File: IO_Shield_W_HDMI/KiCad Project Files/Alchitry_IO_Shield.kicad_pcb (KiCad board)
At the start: 4 copper layers, 65 x 45 mm, 67 parts, among them J1 HDMI_A_1.4, Q1 Q_PMOS_SGD, Q2 Q_PMOS_SGD, Q3 Q_PMOS_SGD, SW1 SW_DIP_x08, SW2 SW_DIP_x08, U1 boardmezzanine_new, U2 TFP410

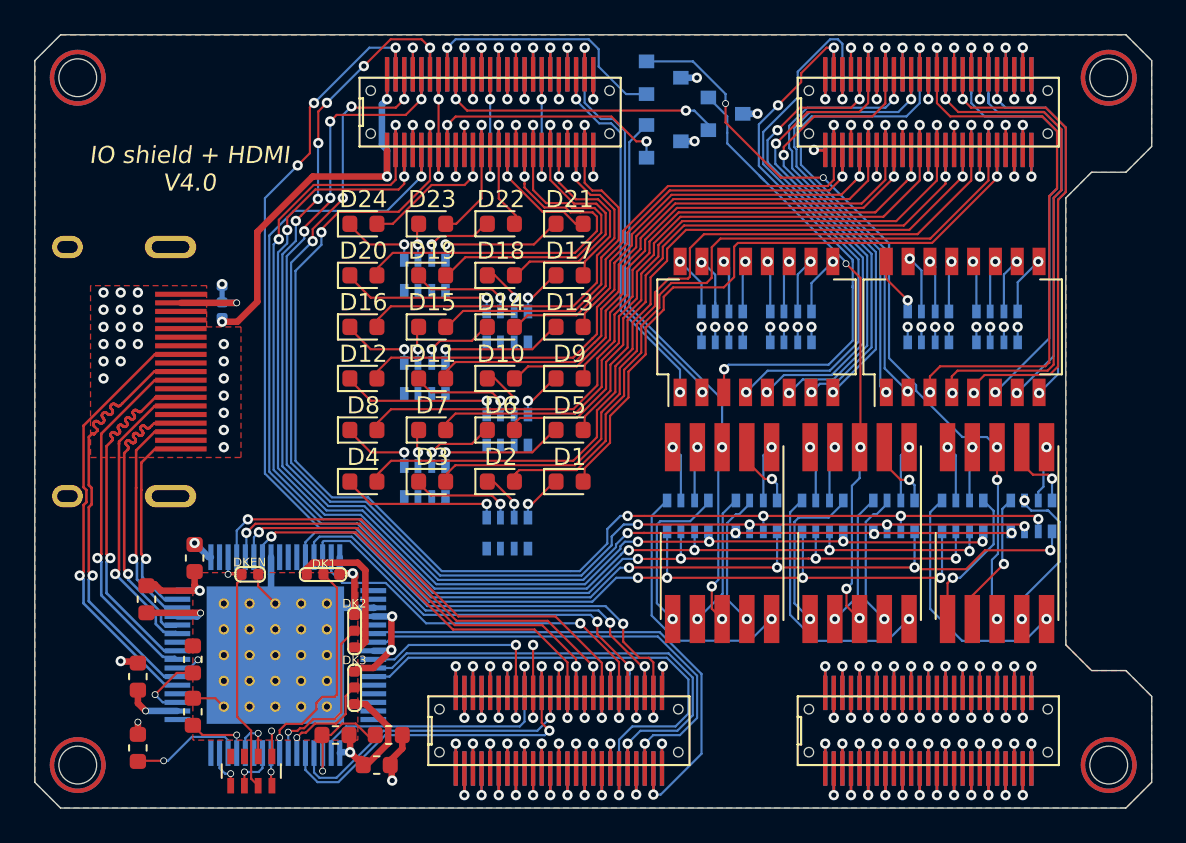
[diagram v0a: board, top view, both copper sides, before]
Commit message: fixed dirll sizes
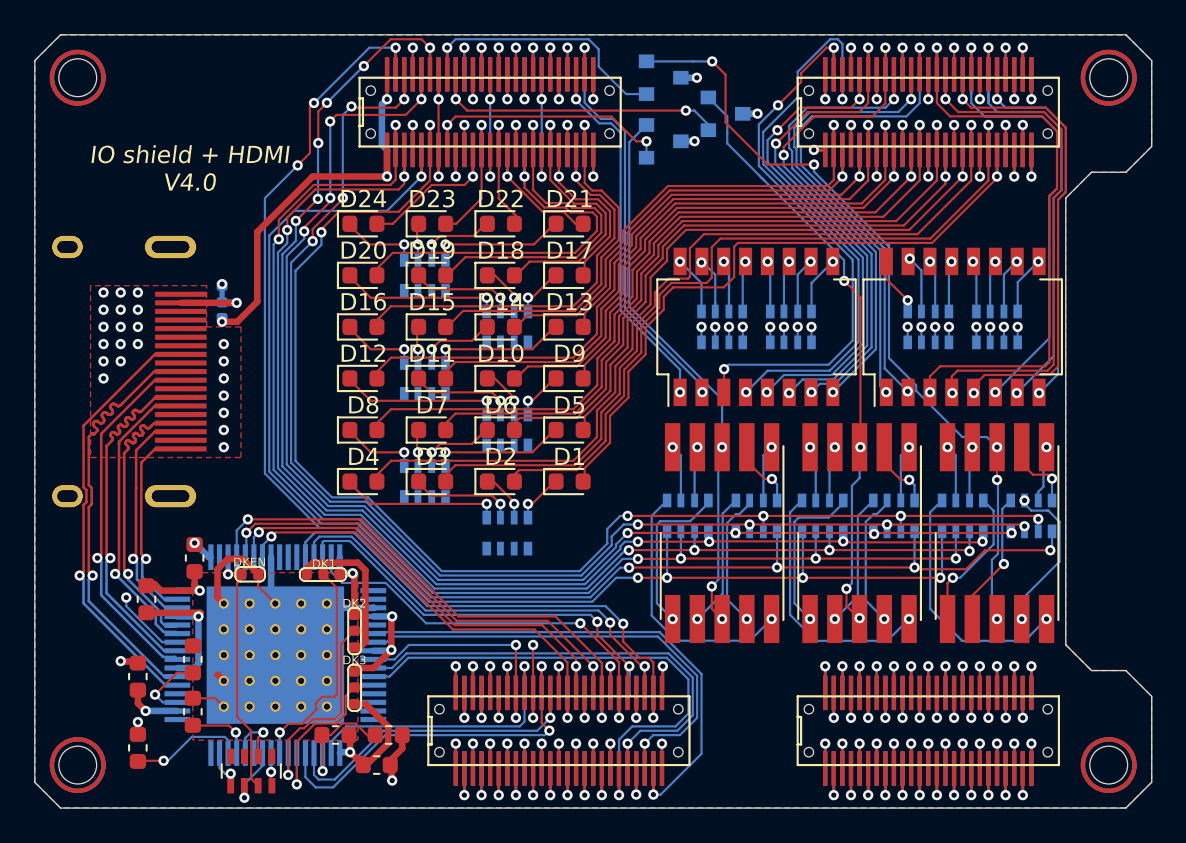
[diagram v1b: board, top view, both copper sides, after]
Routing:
- net GNDREF: track 120.3 -> 130.3 mm, vias 62 -> 63
- net /HDMI/DK3: track 6.07 -> 9.58 mm
- net /HDMI/DK2: track 9.84 -> 12.1 mm
- net /HDMI/ISEL: track 3.83 -> 4.94 mm
- net Net-(RN1-Pad6): track 2.82 -> 3.73 mm
- net /HDMI/DK1: track 13.1 -> 13.9 mm
- net Net-(AFF1-Pad3): track 45.5 -> 46.3 mm
- net +3V3: track 151.6 -> 152.2 mm, vias 57 -> 55
